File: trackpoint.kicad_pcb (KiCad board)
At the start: 2 copper layers, 27.5 x 34.5 mm, 11 parts

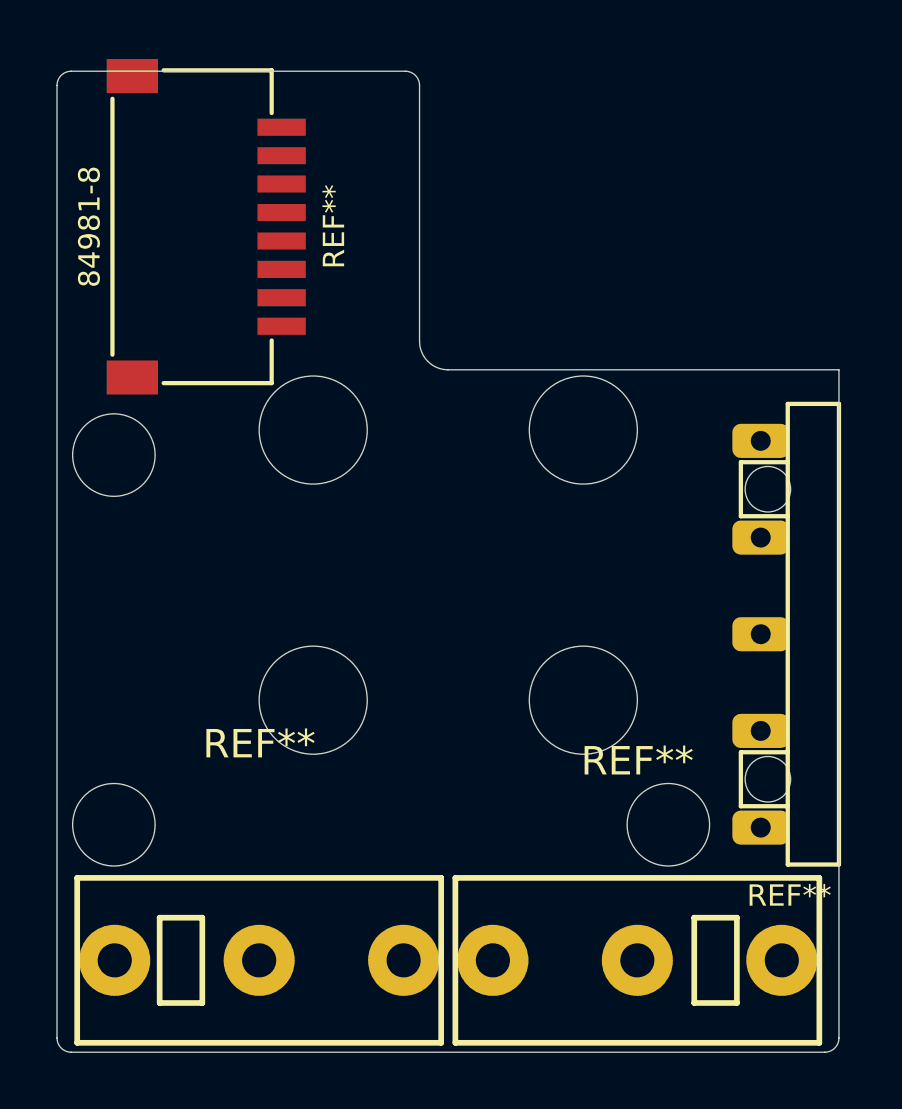
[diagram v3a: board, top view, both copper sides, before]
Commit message: Improve silk screen.
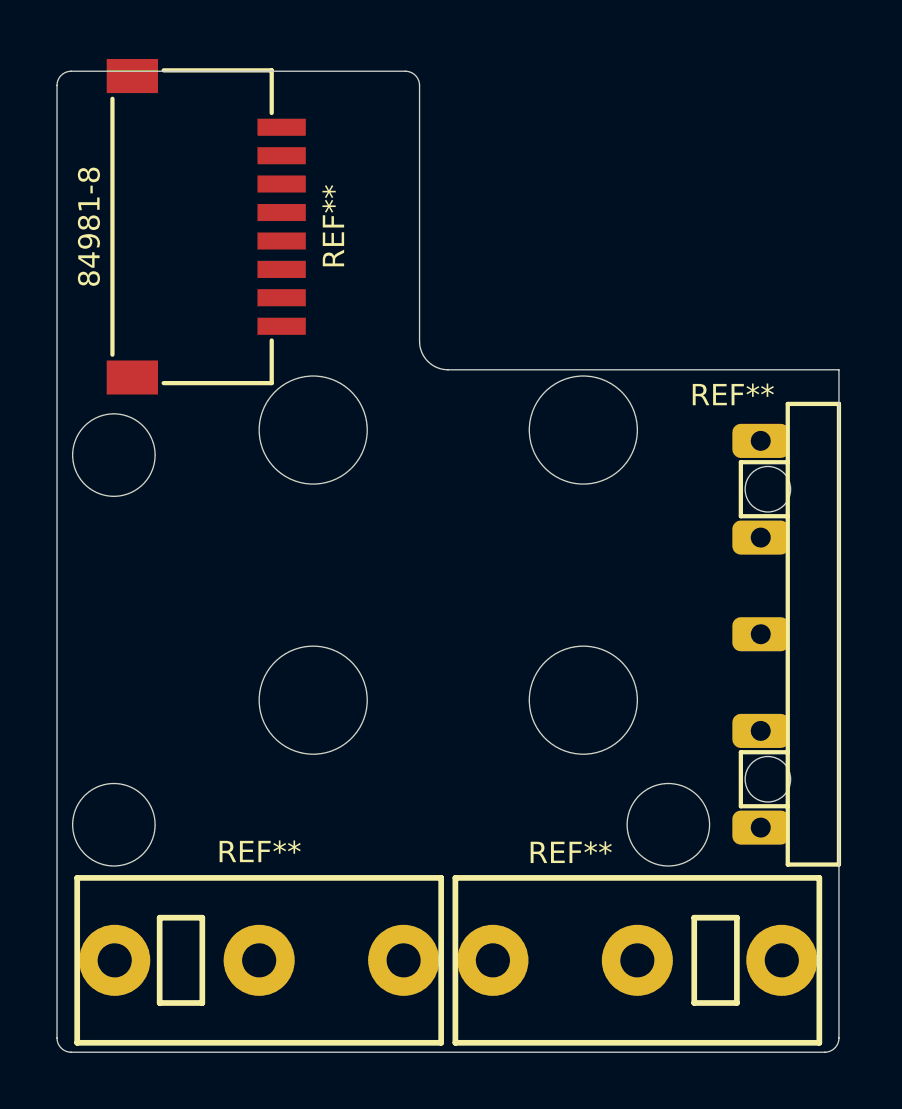
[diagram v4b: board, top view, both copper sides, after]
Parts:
- ? (x4): moved to F.Cu
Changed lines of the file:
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@@
   (general
     (thickness 1.6)
-    (drawings 19)
+    (drawings 15)
     (tracks 0)
     (zones 0)
-    (modules 7)
+    (modules 11)
     (nets 1)
   )
@@
     (uvia_drill 0.127)
   )
+  (module ugl:CMI126603D08 locked (layer F.Cu)
+    (at 199.360001 144.268997)
+    (fp_text reference REF** (at 0 -3.8) (layer F.SilkS)
+      (effects (font (size 0.75 0.75) (thickness 0.15)))
+    )
+    (fp_text value CMI126603D08 (at 0 3.9) (layer F.Fab)
+      (effects (font (size 0.75 0.75) (thickness 0.15)))
+    )
+    (fp_line (start -3.5 1.5) (end -3.5 -1.5) (layer F.SilkS) (width 0.2))
+    (fp_line (start -2 1.5) (end -3.5 1.5) (layer F.SilkS) (width 0.2))
+    (fp_line (start -2 -1.5) (end -2 1.5) (layer F.SilkS) (width 0.2))
+    (fp_line (start -3.5 -1.5) (end -2 -1.5) (layer F.SilkS) (width 0.2))
+    (fp_line (start 6.4 -2.9) (end 6.4 2.9) (layer F.SilkS) (width 0.2))
+    (fp_line (start -6.4 2.9) (end 6.4 2.9) (layer F.SilkS) (width 0.2))
+    (fp_line (start -6.4 -2.9) (end -6.4 2.9) (layer F.SilkS) (width 0.2))
+    (fp_line (start 6.4 -2.9) (end -6.4 -2.9) (layer F.SilkS) (width 0.2))
+    (pad 3 thru_hole circle (at 5.08 0) (size 2.5 2.5) (drill 1.2) (layers *.Cu *.Mask))
+    (pad 2 thru_hole circle (at 0 0) (size 2.5 2.5) (drill 1.2) (layers *.Cu *.Mask))
+    (pad 1 thru_hole circle (at -5.08 0) (size 2.5 2.5) (drill 1.2) (layers *.Cu *.Mask))
+  )
+  (module ugl:CMI126603D08 locked (layer F.Cu)
+    (at 212.660004 144.268997 180)
+    (fp_text reference REF** (at 2.360004 3.768997) (layer F.SilkS)
+      (effects (font (size 0.75 0.75) (thickness 0.15)))
+    )
+    (fp_text value CMI126603D08 (at 0 3.9) (layer F.Fab)
+      (effects (font (size 0.75 0.75) (thickness 0.15)))
+    )
+    (fp_line (start -3.5 1.5) (end -3.5 -1.5) (layer F.SilkS) (width 0.2))
+    (fp_line (start -2 1.5) (end -3.5 1.5) (layer F.SilkS) (width 0.2))
+    (fp_line (start -2 -1.5) (end -2 1.5) (layer F.SilkS) (width 0.2))
+    (fp_line (start -3.5 -1.5) (end -2 -1.5) (layer F.SilkS) (width 0.2))
+    (fp_line (start 6.4 -2.9) (end 6.4 2.9) (layer F.SilkS) (width 0.2))
+    (fp_line (start -6.4 2.9) (end 6.4 2.9) (layer F.SilkS) (width 0.2))
+    (fp_line (start -6.4 -2.9) (end -6.4 2.9) (layer F.SilkS) (width 0.2))
+    (fp_line (start 6.4 -2.9) (end -6.4 -2.9) (layer F.SilkS) (width 0.2))
+    (pad 3 thru_hole circle (at 5.08 0 180) (size 2.5 2.5) (drill 1.2) (layers *.Cu *.Mask))
+    (pad 2 thru_hole circle (at 0 0 180) (size 2.5 2.5) (drill 1.2) (layers *.Cu *.Mask))
+    (pad 1 thru_hole circle (at -5.08 0 180) (size 2.5 2.5) (drill 1.2) (layers *.Cu *.Mask))
+  )
   (module ugl:84981-8 (layer F.Cu)
     (at 194.199997 118.468994 270)
@@
     (pad 2 smd rect (at -2.5 -5.95 270) (size 0.6 1.7) (layers F.Cu F.Paste F.Mask))
   )
-  (module ugl:CMI126603D08 locked (layer F.Cu)
-    (at 199.360001 144.268997)
-    (fp_text reference REF** (at 0 -7.6) (layer F.SilkS)
-      (effects (font (size 1 1) (thickness 0.15)))
-    )
-    (fp_text value CMI126603D08 (at 0 8.8) (layer F.Fab)
-      (effects (font (size 1 1) (thickness 0.15)))
-    )
-    (fp_line (start -3.5 1.5) (end -3.5 -1.5) (layer F.SilkS) (width 0.2))
-    (fp_line (start -2 1.5) (end -3.5 1.5) (layer F.SilkS) (width 0.2))
-    (fp_line (start -2 -1.5) (end -2 1.5) (layer F.SilkS) (width 0.2))
-    (fp_line (start -3.5 -1.5) (end -2 -1.5) (layer F.SilkS) (width 0.2))
-    (fp_line (start 6.4 -2.9) (end 6.4 2.9) (layer F.SilkS) (width 0.2))
-    (fp_line (start -6.4 2.9) (end 6.4 2.9) (layer F.SilkS) (width 0.2))
-    (fp_line (start -6.4 -2.9) (end -6.4 2.9) (layer F.SilkS) (width 0.2))
-    (fp_line (start 6.4 -2.9) (end -6.4 -2.9) (layer F.SilkS) (width 0.2))
-    (pad 3 thru_hole circle (at 5.08 0) (size 2.5 2.5) (drill 1.2) (layers *.Cu *.Mask))
-    (pad 2 thru_hole circle (at 0 0) (size 2.5 2.5) (drill 1.2) (layers *.Cu *.Mask))
-    (pad 1 thru_hole circle (at -5.08 0) (size 2.5 2.5) (drill 1.2) (layers *.Cu *.Mask))
-  )
   (module ugl:UHK_Male_Pogo_Pin_v2 locked (layer F.Cu)
     (at 219.75 132.800003)
     (attr virtual)
-    (fp_text reference REF** (at -1.75 9.199997) (layer F.SilkS)
+    (fp_text reference REF** (at -3.75 -8.400003) (layer F.SilkS)
       (effects (font (size 0.75 0.75) (thickness 0.15)))
     )
@@
       (clearance 0.00254))
   )
-  (module ugl:CMI126603D08 locked (layer F.Cu)
-    (at 212.660004 144.268997 180)
-    (fp_text reference REF** (at 0 7) (layer F.SilkS)
-      (effects (font (size 1 1) (thickness 0.15)))
-    )
-    (fp_text value CMI126603D08 (at 0 8.8) (layer F.Fab)
-      (effects (font (size 1 1) (thickness 0.15)))
-    )
-    (fp_line (start 6.4 -2.9) (end -6.4 -2.9) (layer F.SilkS) (width 0.2))
-    (fp_line (start -6.4 -2.9) (end -6.4 2.9) (layer F.SilkS) (width 0.2))
-    (fp_line (start -6.4 2.9) (end 6.4 2.9) (layer F.SilkS) (width 0.2))
-    (fp_line (start 6.4 -2.9) (end 6.4 2.9) (layer F.SilkS) (width 0.2))
-    (fp_line (start -3.5 -1.5) (end -2 -1.5) (layer F.SilkS) (width 0.2))
-    (fp_line (start -2 -1.5) (end -2 1.5) (layer F.SilkS) (width 0.2))
-    (fp_line (start -2 1.5) (end -3.5 1.5) (layer F.SilkS) (width 0.2))
-    (fp_line (start -3.5 1.5) (end -3.5 -1.5) (layer F.SilkS) (width 0.2))
-    (pad 1 thru_hole circle (at -5.08 0 180) (size 2.5 2.5) (drill 1.2) (layers *.Cu *.Mask))
-    (pad 2 thru_hole circle (at 0 0 180) (size 2.5 2.5) (drill 1.2) (layers *.Cu *.Mask))
-    (pad 3 thru_hole circle (at 5.08 0 180) (size 2.5 2.5) (drill 1.2) (layers *.Cu *.Mask))
-  )
   (module UGL:hole_2.9000000953674316mm locked (layer F.Cu)
     (at 194.25 126.5)
@@
     )
     (pad "" np_thru_hole circle (at 0 0) (size 2.9 2.9) (drill 2.9) (layers *.Cu *.Mask F.SilkS)
+      (clearance 0.00001))
+  )
+  (module UGL:hole_3.8000000000000114mm locked (layer F.Cu)
+    (at 210.760002 135.119003)
+    (attr virtual)
+    (fp_text reference "" (at 0 0) (layer F.SilkS)
+      (effects (font (size 1.27 1.27) (thickness 0.15)))
+    )
+    (fp_text value "" (at 0 0) (layer F.SilkS)
+      (effects (font (size 1.27 1.27) (thickness 0.15)))
+    )
+    (pad "" np_thru_hole circle (at 0 0) (size 3.8 3.8) (drill 3.8) (layers *.Cu *.Mask F.SilkS)
+      (clearance 0.00001))
+  )
+  (module UGL:hole_3.8000000000000114mm locked (layer F.Cu)
+    (at 201.260002 135.119003)
+    (attr virtual)
+    (fp_text reference "" (at 0 0) (layer F.SilkS)
+      (effects (font (size 1.27 1.27) (thickness 0.15)))
+    )
+    (fp_text value "" (at 0 0) (layer F.SilkS)
+      (effects (font (size 1.27 1.27) (thickness 0.15)))
+    )
+    (pad "" np_thru_hole circle (at 0 0) (size 3.8 3.8) (drill 3.8) (layers *.Cu *.Mask F.SilkS)
+      (clearance 0.00001))
+  )
+  (module UGL:hole_3.799999999999983mm locked (layer F.Cu)
+    (at 201.260002 125.619003)
+    (attr virtual)
+    (fp_text reference "" (at 0 0) (layer F.SilkS)
+      (effects (font (size 1.27 1.27) (thickness 0.15)))
+    )
+    (fp_text value "" (at 0 0) (layer F.SilkS)
+      (effects (font (size 1.27 1.27) (thickness 0.15)))
+    )
+    (pad "" np_thru_hole circle (at 0 0) (size 3.8 3.8) (drill 3.8) (layers *.Cu *.Mask F.SilkS)
+      (clearance 0.00001))
+  )
+  (module UGL:hole_3.799999999999983mm locked (layer F.Cu)
+    (at 210.760002 125.619003)
+    (attr virtual)
+    (fp_text reference "" (at 0 0) (layer F.SilkS)
+      (effects (font (size 1.27 1.27) (thickness 0.15)))
+    )
+    (fp_text value "" (at 0 0) (layer F.SilkS)
+      (effects (font (size 1.27 1.27) (thickness 0.15)))
+    )
+    (pad "" np_thru_hole circle (at 0 0) (size 3.8 3.8) (drill 3.8) (layers *.Cu *.Mask F.SilkS)
       (clearance 0.00001))
   )
@@
   (gr_arc (start 219.25 146.999993) (end 219.25 147.5) (angle -90.00451968) (layer Edge.Cuts) (width 0.01))
   (gr_line (start 192.75 147.5) (end 219.25 147.5) (angle 90) (layer Edge.Cuts) (width 0.01))
-  (module UGL:hole_3.8000000000000114mm locked (layer F.Adhes)
-    (at 210.760002 135.119003)
-    (attr virtual)
-    (pad "" np_thru_hole circle (at 0 0) (size 3.8000000000000114 3.8000000000000114) (drill 3.8000000000000114) (layers *.Cu *.Mask F.SilkS)
-      (clearance 0.00001)
-    )
-  )
-  (module UGL:hole_3.8000000000000114mm locked (layer F.Adhes)
-    (at 201.260002 135.119003)
-    (attr virtual)
-    (pad "" np_thru_hole circle (at 0 0) (size 3.8000000000000114 3.8000000000000114) (drill 3.8000000000000114) (layers *.Cu *.Mask F.SilkS)
-      (clearance 0.00001)
-    )
-  )
   (gr_circle (center 194.25 139.5) (end 195.9 139.5) (layer Eco1.User) (width 0.01))
   (gr_circle (center 213.75 139.5) (end 215.4 139.5) (layer Eco1.User) (width 0.01))
   (gr_circle (center 194.25 126.5) (end 195.9 126.5) (layer Eco1.User) (width 0.01))
-  (module UGL:hole_3.799999999999983mm locked (layer F.Adhes)
-    (at 201.260002 125.619003)
-    (attr virtual)
-    (pad "" np_thru_hole circle (at 0 0) (size 3.799999999999983 3.799999999999983) (drill 3.799999999999983) (layers *.Cu *.Mask F.SilkS)
-      (clearance 0.00001)
-    )
-  )
-  (module UGL:hole_3.799999999999983mm locked (layer F.Adhes)
-    (at 210.760002 125.619003)
-    (attr virtual)
-    (pad "" np_thru_hole circle (at 0 0) (size 3.799999999999983 3.799999999999983) (drill 3.799999999999983) (layers *.Cu *.Mask F.SilkS)
-      (clearance 0.00001)
-    )
-  )
   (gr_arc (start 205.999992 122.500001) (end 205 122.5) (angle -90) (layer Edge.Cuts) (width 0.01))
   (gr_line (start 205 122.5) (end 205 113.5) (angle 90) (layer Edge.Cuts) (width 0.01))

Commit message: Fix hole diameters. Lock FFC connector.
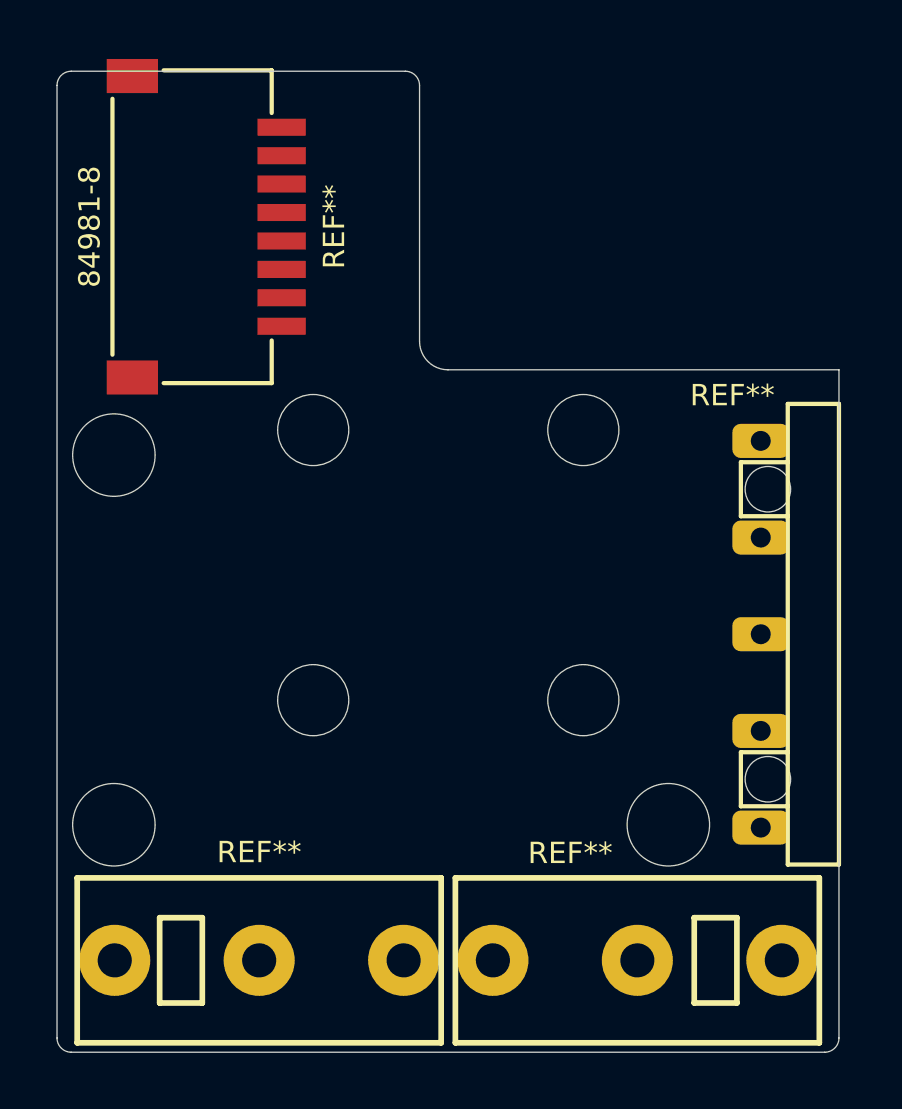
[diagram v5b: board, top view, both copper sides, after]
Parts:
- removed the ? at (210.8, 135.1)
- removed the ? at (201.3, 135.1)
- removed the ? at (201.3, 125.6)
- removed the ? at (210.8, 125.6)
- added ?: , UGL:hole_2.5mm, F.Cu at (210.8, 135.1)
- added ?: , UGL:hole_2.5mm, F.Cu at (201.3, 135.1)
- added ?: , UGL:hole_2.5mm, F.Cu at (201.3, 125.6)
- added ?: , UGL:hole_2.5mm, F.Cu at (210.8, 125.6)
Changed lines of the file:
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@@
       (clearance 0.00001))
   )
-  (module UGL:hole_3.8000000000000114mm locked (layer F.Cu)
+  (module UGL:hole_2.5mm locked (layer F.Cu)
     (at 210.760002 135.119003)
     (attr virtual)
@@
       (effects (font (size 1.27 1.27) (thickness 0.15)))
     )
-    (pad "" np_thru_hole circle (at 0 0) (size 3.8 3.8) (drill 3.8) (layers *.Cu *.Mask F.SilkS)
+    (pad "" np_thru_hole circle (at 0 0) (size 2.5 2.5) (drill 2.5) (layers *.Cu *.Mask F.SilkS)
       (clearance 0.00001))
   )
-  (module UGL:hole_3.8000000000000114mm locked (layer F.Cu)
+  (module UGL:hole_2.5mm locked (layer F.Cu)
     (at 201.260002 135.119003)
     (attr virtual)
@@
       (effects (font (size 1.27 1.27) (thickness 0.15)))
     )
-    (pad "" np_thru_hole circle (at 0 0) (size 3.8 3.8) (drill 3.8) (layers *.Cu *.Mask F.SilkS)
+    (pad "" np_thru_hole circle (at 0 0) (size 2.5 2.5) (drill 2.5) (layers *.Cu *.Mask F.SilkS)
       (clearance 0.00001))
   )
-  (module UGL:hole_3.799999999999983mm locked (layer F.Cu)
+  (module UGL:hole_2.5mm locked (layer F.Cu)
     (at 201.260002 125.619003)
     (attr virtual)
@@
       (effects (font (size 1.27 1.27) (thickness 0.15)))
     )
-    (pad "" np_thru_hole circle (at 0 0) (size 3.8 3.8) (drill 3.8) (layers *.Cu *.Mask F.SilkS)
+    (pad "" np_thru_hole circle (at 0 0) (size 2.5 2.5) (drill 2.5) (layers *.Cu *.Mask F.SilkS)
       (clearance 0.00001))
   )
-  (module UGL:hole_3.799999999999983mm locked (layer F.Cu)
+  (module UGL:hole_2.5mm locked (layer F.Cu)
     (at 210.760002 125.619003)
     (attr virtual)
@@
       (effects (font (size 1.27 1.27) (thickness 0.15)))
     )
-    (pad "" np_thru_hole circle (at 0 0) (size 3.8 3.8) (drill 3.8) (layers *.Cu *.Mask F.SilkS)
+    (pad "" np_thru_hole circle (at 0 0) (size 2.5 2.5) (drill 2.5) (layers *.Cu *.Mask F.SilkS)
       (clearance 0.00001))
   )

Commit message: Update the outline so that the pads of the FFC connector fit.
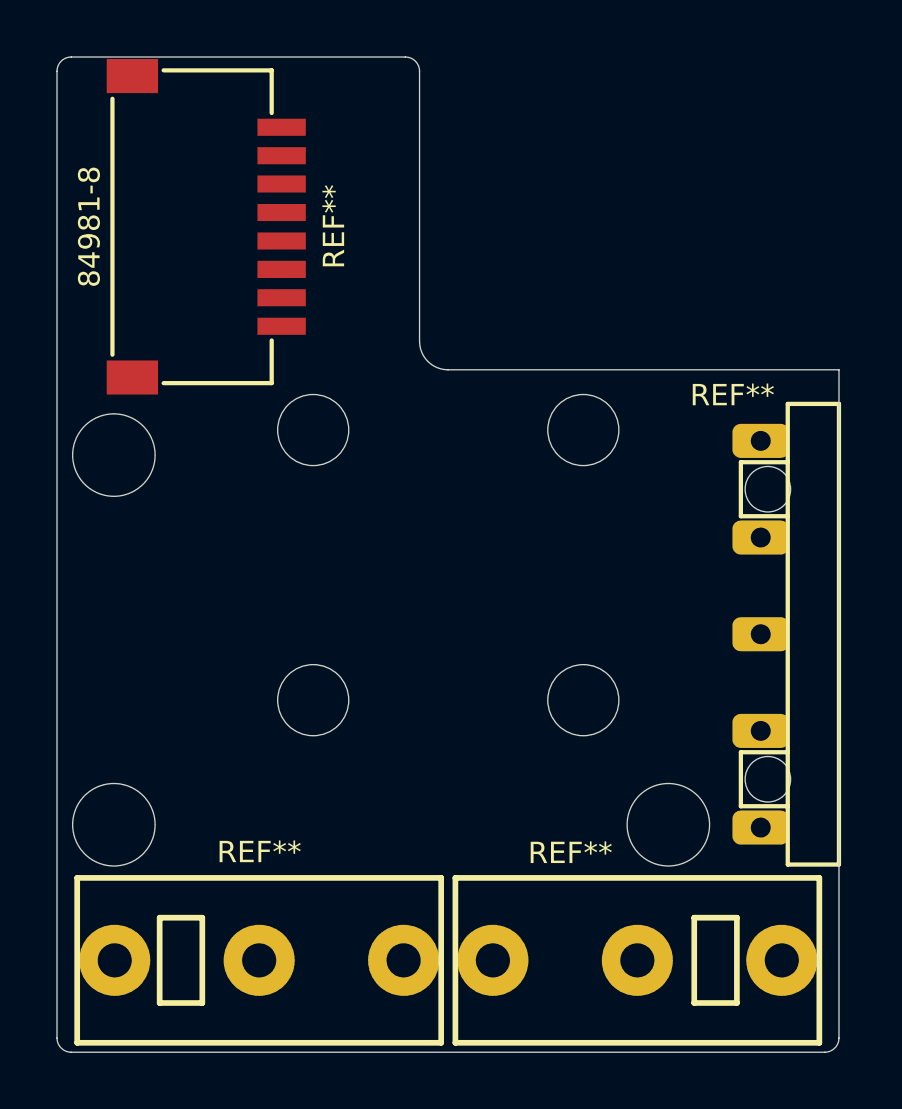
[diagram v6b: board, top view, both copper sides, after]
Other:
- board size 27.5 x 34.5 mm -> 27.5 x 35 mm
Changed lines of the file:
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@@
       (clearance 0.00001))
   )
-  (gr_line (start 204.5 113) (end 192.75 113) (angle 90) (layer Edge.Cuts) (width 0.01))
-  (gr_line (start 192.25 113.5) (end 192.25 147) (angle 90) (layer Edge.Cuts) (width 0.01))
+  (gr_line (start 204.5 112.5) (end 192.75 112.5) (angle 90) (layer Edge.Cuts) (width 0.01))
+  (gr_line (start 192.25 113) (end 192.25 147) (angle 90) (layer Edge.Cuts) (width 0.01))
   (gr_line (start 219.75 123.5) (end 206 123.5) (angle 90) (layer Edge.Cuts) (width 0.01))
   (gr_text "PCB ID: trackpoint_main_0.1.0" (at 206.1 146.5) (layer B.SilkS)
@@
   (gr_circle (center 194.25 126.5) (end 195.9 126.5) (layer Eco1.User) (width 0.01))
   (gr_arc (start 205.999992 122.500001) (end 205 122.5) (angle -90) (layer Edge.Cuts) (width 0.01))
-  (gr_line (start 205 122.5) (end 205 113.5) (angle 90) (layer Edge.Cuts) (width 0.01))
-  (gr_arc (start 204.5 113.500007) (end 205 113.5) (angle -90) (layer Edge.Cuts) (width 0.01))
-  (gr_arc (start 192.75 113.500007) (end 192.75 113) (angle -90) (layer Edge.Cuts) (width 0.01))
+  (gr_line (start 205 122.5) (end 205 113) (angle 90) (layer Edge.Cuts) (width 0.01))
+  (gr_arc (start 204.500007 113) (end 205.000007 112.999993) (angle -90) (layer Edge.Cuts) (width 0.01))
+  (gr_arc (start 192.75 113.000007) (end 192.75 112.5) (angle -90) (layer Edge.Cuts) (width 0.01))
   (gr_line (start 219.75 147) (end 219.75 123.5) (angle 90) (layer Edge.Cuts) (width 0.01))
 )
